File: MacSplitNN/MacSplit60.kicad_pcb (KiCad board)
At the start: 2 copper layers, 166.1 x 112 mm, 73 parts, among them J1 USB_C_Receptacle_USB2.0, SW1 SW_Push, SW10 SW_Push, SW100 SW_SPST, SW11 SW_Push, SW12 SW_Push, SW13 SW_Push, SW14 SW_Push, SW15 SW_Push, SW16 SW_Push, SW17 SW_Push, SW18 SW_Push, SW19 SW_Push, SW2 SW_Push, SW20 SW_Push, SW21 SW_Push, SW22 SW_Push, SW23 SW_Push, SW24 SW_Push, SW25 SW_Push, SW26 SW_Push, SW27 SW_Push, SW28 SW_Push, SW29 SW_Push, SW3 SW_Push, SW30 SW_Push, SW4 SW_Push, SW5 SW_Push, SW6 SW_Push, SW7 SW_Push, SW8 SW_Push, SW9 SW_Push, U1 Pico, U2 MCP23S17_ML

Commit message: Modify switches footprints, TRRS board to board
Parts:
- removed C2: C, Capacitor_SMD:C_0603_1608Metric
- removed J1: USB_C_Receptacle_USB2.0, Connector_USB:USB_C_Receptacle_GCT_USB4085_Circular
- removed SW100: SW_SPST, Button_Switch_SMD:SW_SPST_CK_RS282G05A3
- removed U1: Pico, MCU_RaspberryPi_and_Boards:RPi_Pico_SMD_TH
- added JP1: Left/Right, Jumper:SolderJumper-2_P1.3mm_Open_TrianglePad1.0x1.5mm, F.Cu at (202.0, 42.1)
- added JP2: Choice, Jumper:SolderJumper-2_P1.3mm_Open_TrianglePad1.0x1.5mm, F.Cu at (206.3, 42.1)
- U2: value MCP23S17_ML -> KB2040; footprint Package_DFN_QFN:QFN-28-1EP_6x6mm_P0.65mm_EP4.25x4.25mm -> KB2040:Adafruit_KB2040; moved to F.Cu
- moved U2 34.4 mm to (238.0, 43.4)
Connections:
- R1 pad 1: Net-(R1-Pad1) -> Net-(U2-Pad25)
- U2 pad 1: /ROW_4 -> unconnected-(U2-Pad1)
- U2 pad 10: /SPI0_RX -> Net-(U2-Pad10)
- U2 pad 11: GND -> /ROW_4
- U2 pad 12: GND -> /ROW_3
- U2 pad 13: GND -> /ROW_2
- U2 pad 14: /~{RESET} -> /ROW_1
- U2 pad 15: /INTB -> /ROW_0
- U2 pad 16: /INTA -> /COL_5
- U2 pad 17: /COL_0 -> /COL_4
- U2 pad 18: /COL_1 -> /COL_3
- U2 pad 2: unconnected-(U2-Pad2) -> /UART0_TX
- U2 pad 20: /COL_3 -> /COL_1
- U2 pad 21: /COL_4 -> /COL_0
- U2 pad 22: /COL_5 -> unconnected-(U2-Pad22)
- U2 pad 24: unconnected-(U2-Pad24) -> GND
- U2 pad 25: /ROW_0 -> Net-(U2-Pad25)
- U2 pad 26: /ROW_1 -> unconnected-(U2-Pad26)
- U2 pad 3: unconnected-(U2-Pad3) -> /UART0_RX
- U2 pad 4: unconnected-(U2-Pad4) -> GND
- U2 pad 5: +VDC -> GND
- U2 pad 6: GND -> /I2C1_SCK
- U2 pad 7: /SPI0_CSn -> /I2C1_SDA
- U2 pad 8: /SPI0_SCK -> Net-(U2-Pad8)
- U2 pad 9: /SPI0_TX -> Net-(U2-Pad9)
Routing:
- net /ROW_4: track 298.9 -> 0.00 mm
- net /COL_0: track 276.6 -> 0.00 mm
- net /COL_1: track 244.8 -> 0.00 mm, vias 3 -> 2
- net /COL_5: track 235.1 -> 0.00 mm
- net /COL_2: track 222.6 -> 0.00 mm, vias 3 -> 2
- net /COL_4: track 213.9 -> 0.00 mm
- net /COL_3: track 199.7 -> 0.00 mm, vias 3 -> 2
- net /ROW_3: track 192.2 -> 0.00 mm
- net /ROW_0: track 190.1 -> 0.00 mm, vias 10 -> 11
- net /ROW_1: track 163.3 -> 0.00 mm, vias 6 -> 8
- net +VDC: track 159.8 -> 0.00 mm, vias 4 -> 2
- net /ROW_2: track 151.2 -> 0.00 mm
- net /INTA: track 89.6 -> 0.00 mm, vias 3 -> 0
- net /SPI0_RX: track 75.7 -> 0.00 mm
- net /SPI0_SCK: track 71.5 -> 0.00 mm, vias 2 -> 0
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
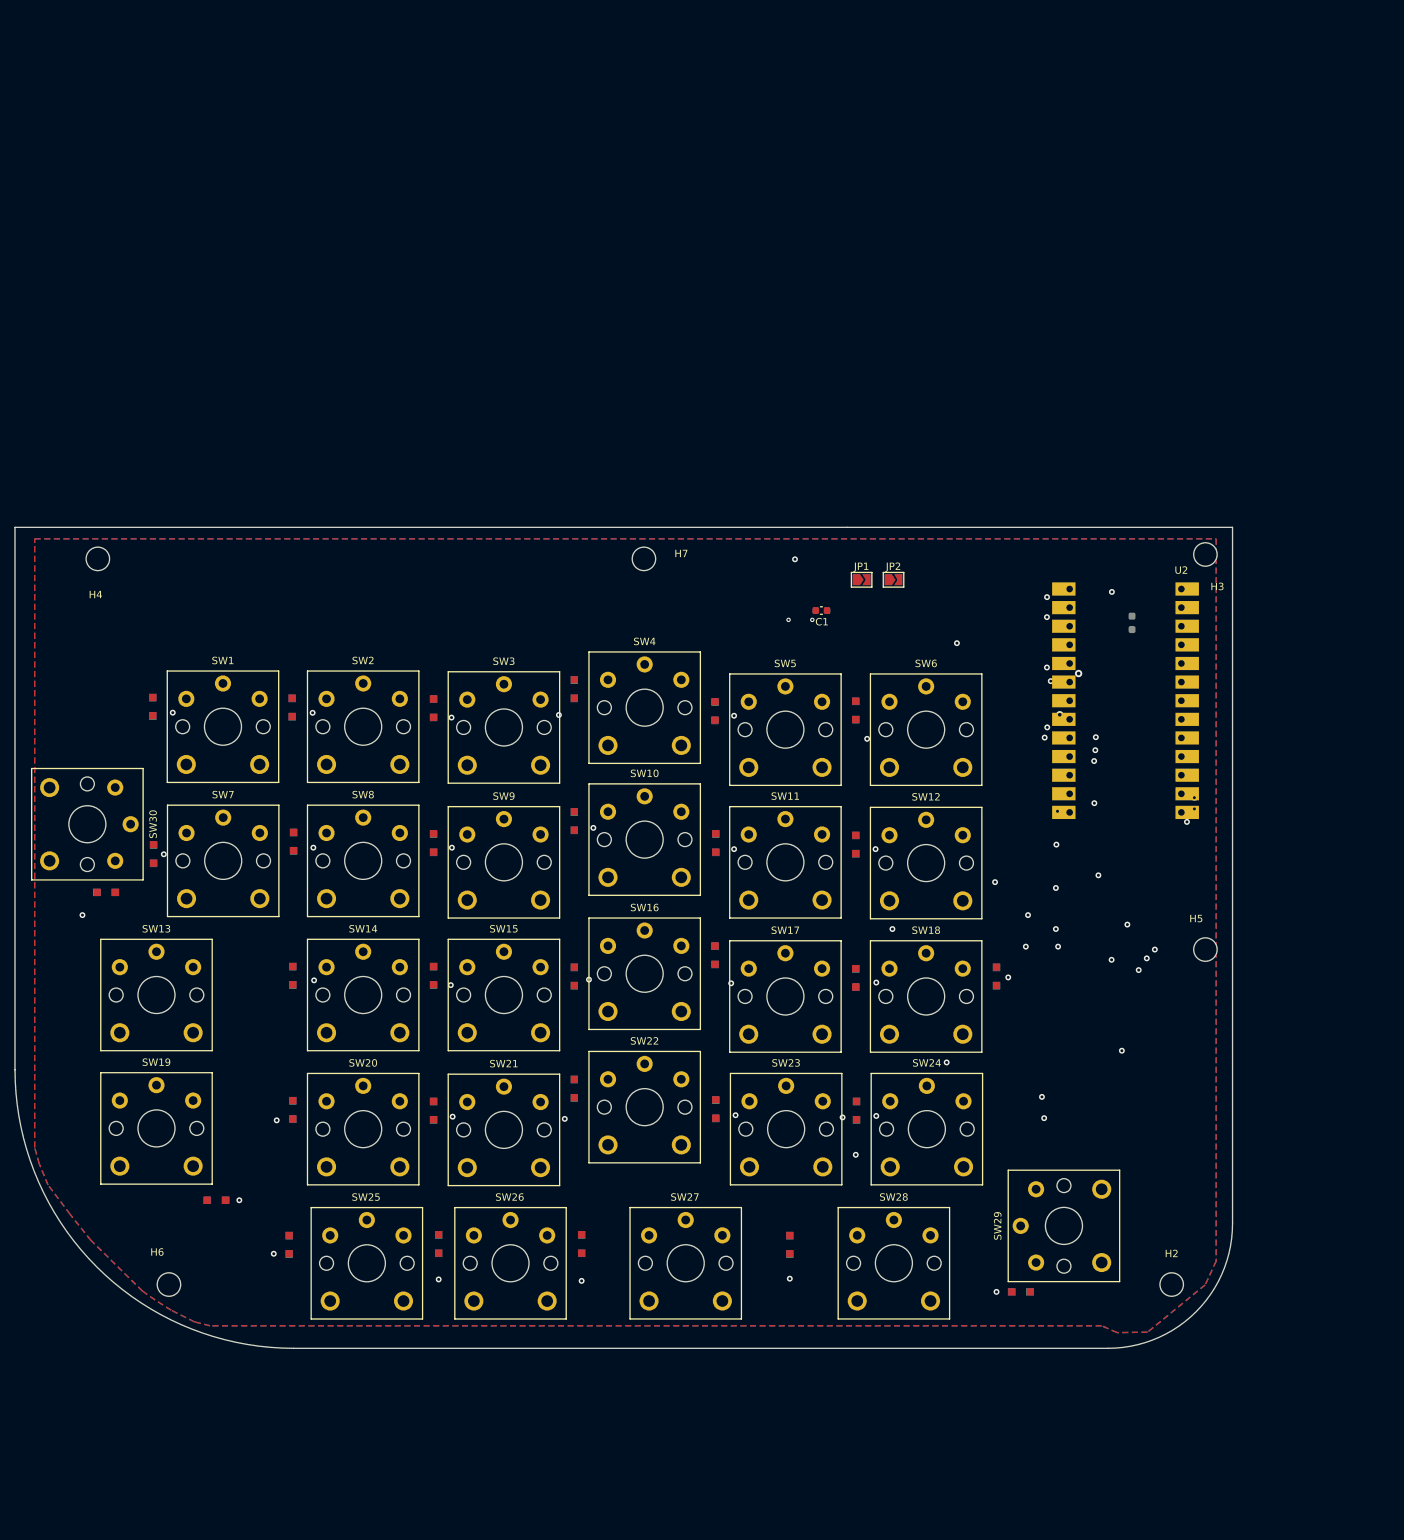
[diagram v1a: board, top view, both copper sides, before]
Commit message: remove all vias, tracks
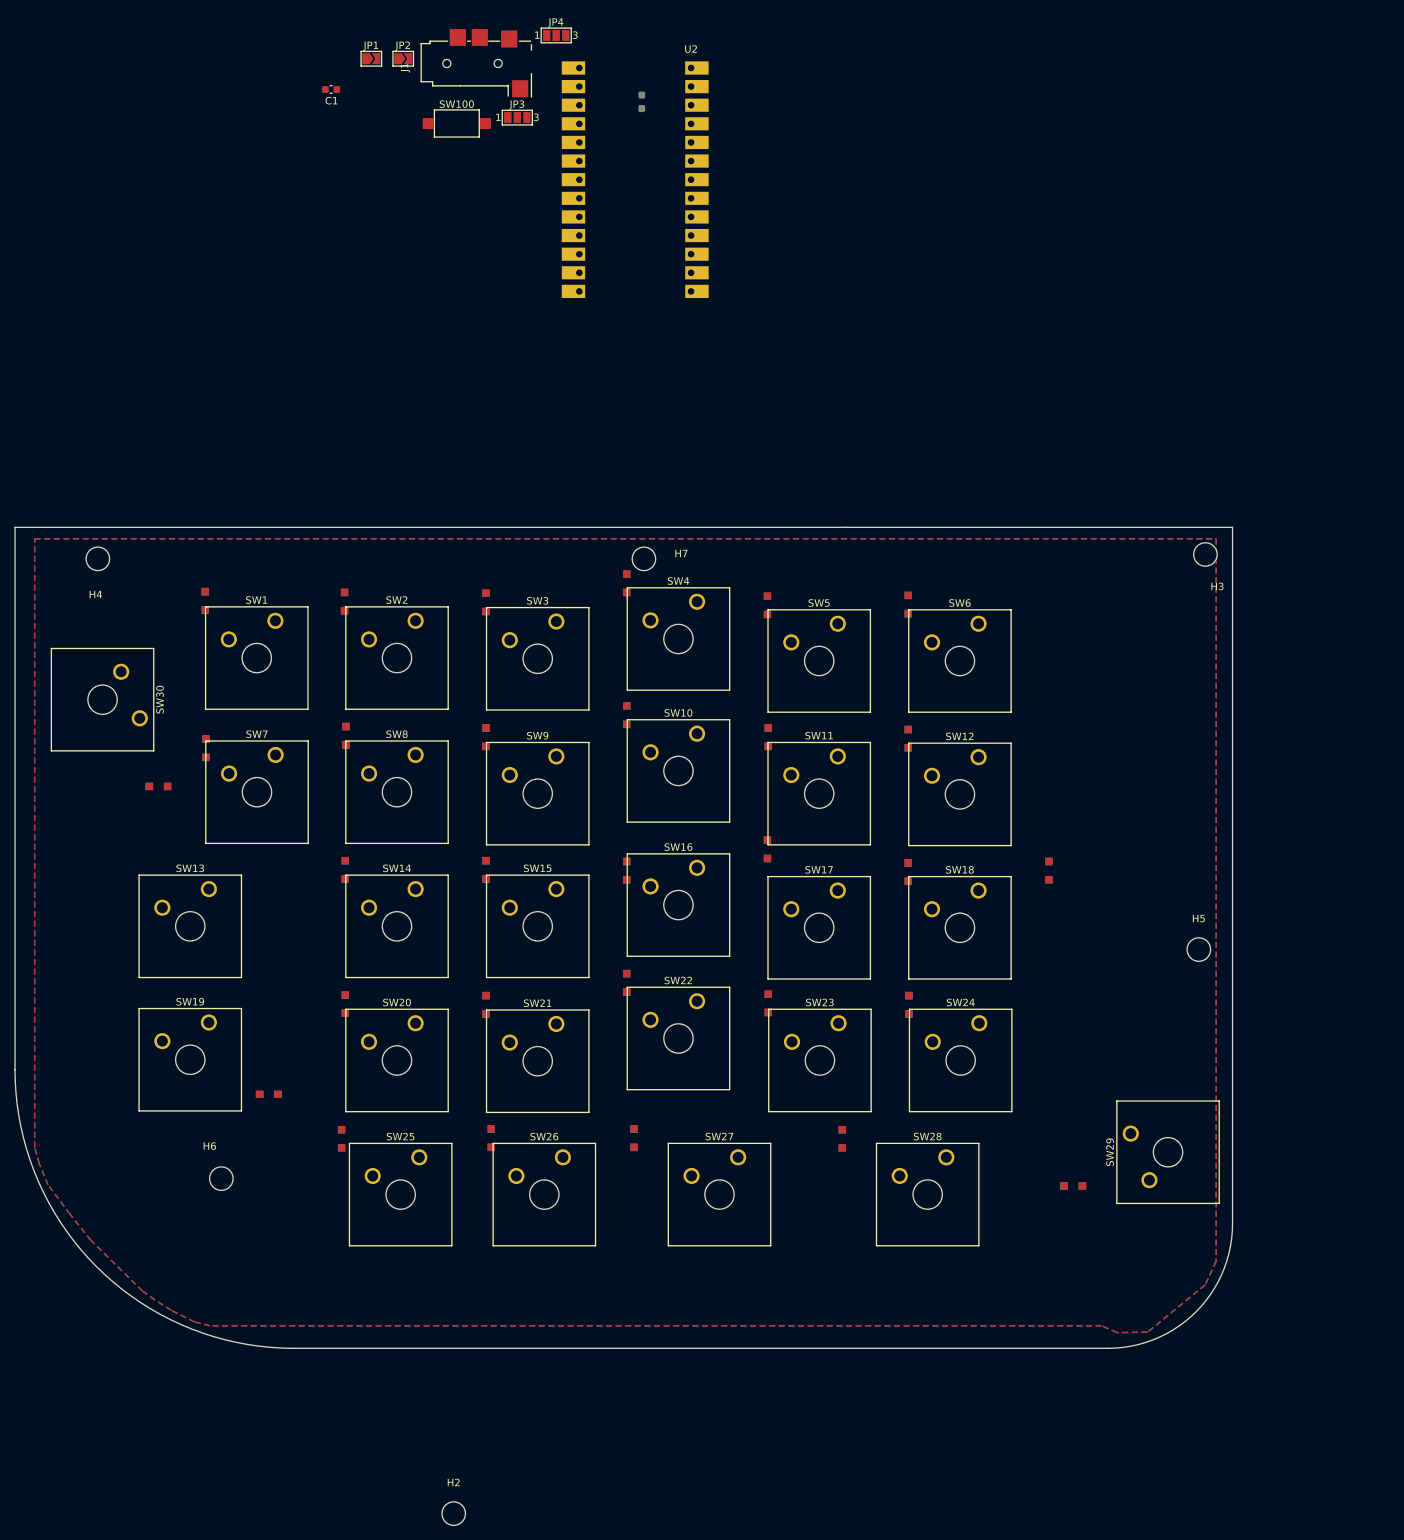
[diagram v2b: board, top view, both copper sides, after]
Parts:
- added J1: AudioJack4, Connector_Audio:Jack_3.5mm_CUI_SJ2-3574A-SMT_Horizontal, F.Cu at (143.1, -28.3)
- added JP3: TX_RP2040, Jumper:SolderJumper-3_P1.3mm_Open_Pad1.0x1.5mm_NumberLabels, F.Cu at (155.0, -20.9)
- added JP4: RX_RP2040, Jumper:SolderJumper-3_P1.3mm_Open_Pad1.0x1.5mm_NumberLabels, F.Cu at (160.3, -32.1)
- added SW100: Toggle Mac/Win, Button_Switch_SMD:SW_SPST_CK_RS282G05A3, F.Cu at (146.8, -20.1)
- SW1, SW10, SW11, SW12, SW14, SW15, SW16, SW17, SW18, SW2, SW20, SW21, SW22, SW23, SW24, SW25, SW26, SW3, SW4, SW5, SW6, SW7, SW8, SW9: footprint Switch_Keyboard_Kailh:SW_Kailh_Choc_V1V2_1.00u -> Button_Switch_Keyboard:SW_Cherry_MX_1.00u_Plate
- SW13, SW19: footprint Switch_Keyboard_Kailh:SW_Kailh_Choc_V1V2_2.00u -> Button_Switch_Keyboard:SW_Cherry_MX_2.00u_Plate
- SW27, SW28, SW29, SW30: footprint Switch_Keyboard_Kailh:SW_Kailh_Choc_V1V2_1.50u -> Button_Switch_Keyboard:SW_Cherry_MX_1.50u_Plate
- moved H2 102.8 mm to (146.3, 169.6)
- moved C1 97.6 mm to (129.6, -24.7)
- moved JP1 97.6 mm to (135.1, -28.9)
- moved JP2 97.6 mm to (139.5, -28.9)
- moved R1 97.6 mm to (172.0, -23.1)
- moved U2 97.6 mm to (171.1, -27.7)
- moved D32 16.1 mm to (230.8, 124.8)
- moved H6 16.1 mm to (114.7, 123.8)
- moved D1 16.1 mm to (112.5, 45.0)
- moved D11 16.1 mm to (131.7, 63.5)
- moved D17 16.1 mm to (150.8, 81.8)
- moved D19 16.1 mm to (189.2, 79.0)
- moved D20 16.1 mm to (208.3, 82.0)
- moved D21 16.1 mm to (227.6, 81.8)
- moved D22 16.1 mm to (121.2, 112.3)
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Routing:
- net Net-(SW100-Pad2): vias 1 -> 0
- net GND: vias 4 -> 0
- net /ROW_4: vias 7 -> 0
- net /ROW_3: vias 7 -> 0
- net /ROW_2: vias 6 -> 0
- net /ROW_1: vias 8 -> 0
- net /ROW_0: vias 11 -> 0
- net /I2C1_SCK: vias 2 -> 0
- net /COL_5: vias 2 -> 0
- net /COL_4: vias 2 -> 0
- net /COL_3: vias 2 -> 0
- net /COL_2: vias 2 -> 0
- net /COL_1: vias 2 -> 0
- net /COL_0: vias 3 -> 0
- net +VDC: vias 2 -> 0
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
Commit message: Update footprint, start repositioning keys
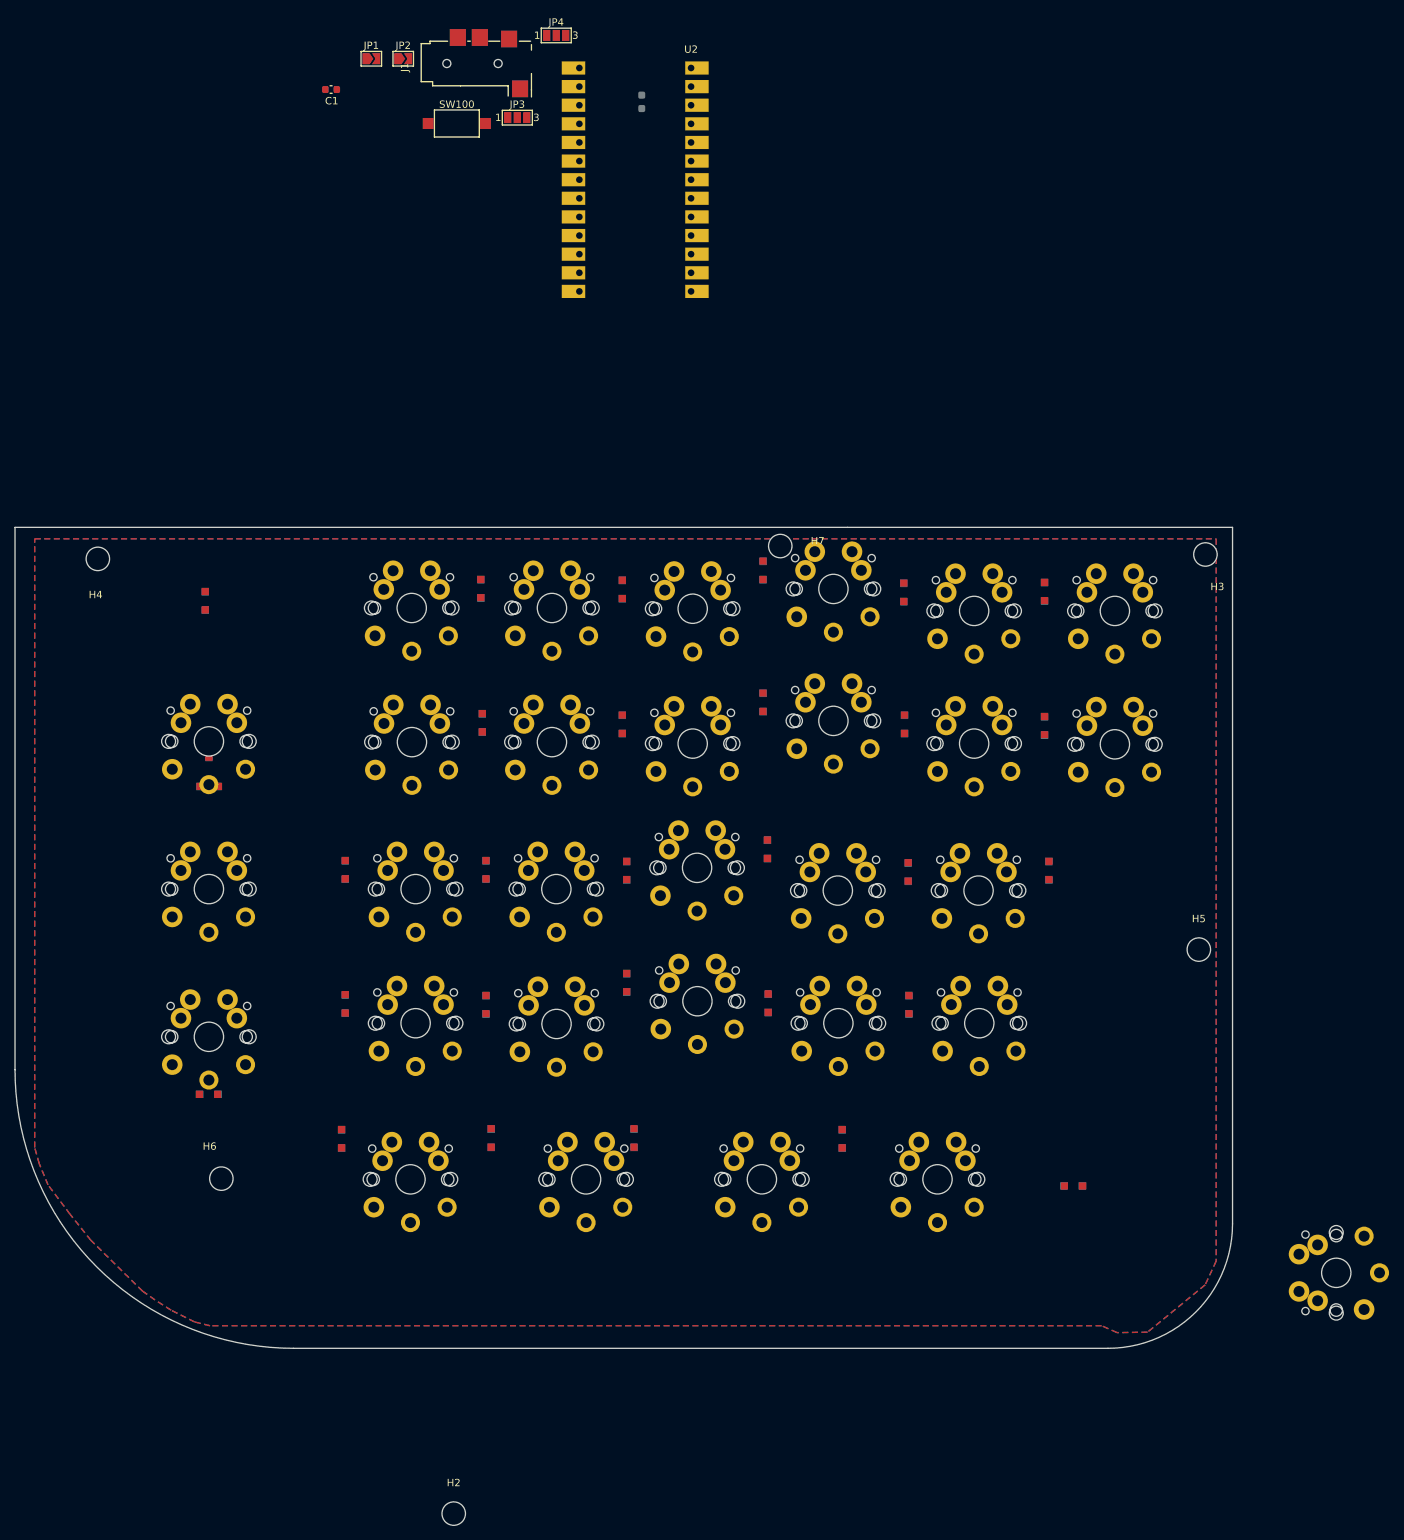
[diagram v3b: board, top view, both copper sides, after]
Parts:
- SW1, SW10, SW11, SW12, SW14, SW15, SW16, SW17, SW18, SW2, SW20, SW21, SW22, SW23, SW24, SW25, SW26, SW3, SW4, SW5, SW6, SW7, SW8, SW9: footprint Button_Switch_Keyboard:SW_Cherry_MX_1.00u_Plate -> Lily58-footprint:MX_PG1350-DoubleSide_Keycap_18mm_1.00u
- SW13, SW19: footprint Button_Switch_Keyboard:SW_Cherry_MX_2.00u_Plate -> Lily58-footprint:MX_PG1350-DoubleSide_Keycap_28mm_1.50u
- SW27, SW28, SW29, SW30: footprint Button_Switch_Keyboard:SW_Cherry_MX_1.50u_Plate -> Lily58-footprint:MX_PG1350-DoubleSide_Keycap_28mm_1.50u
- moved SW29 33.9 mm to (266.8, 136.7)
- moved D13 18.7 mm to (188.5, 58.9)
- moved D15 18.7 mm to (226.9, 62.1)
- moved D2 18.7 mm to (150.1, 43.4)
- moved D4 18.7 mm to (188.5, 40.9)
- moved D6 18.7 mm to (226.9, 43.8)
- moved SW12 18.7 mm to (236.5, 64.6)
- moved SW3 18.7 mm to (178.9, 46.1)
- moved SW6 18.7 mm to (236.5, 46.4)
- moved SW9 18.7 mm to (178.9, 64.5)
- moved SW7 18.7 mm to (140.7, 64.3)
- moved D11 18.7 mm to (150.2, 61.7)
- moved D12 18.7 mm to (169.3, 61.9)
- moved D14 18.7 mm to (207.8, 61.9)
- moved D3 18.7 mm to (169.3, 43.5)
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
